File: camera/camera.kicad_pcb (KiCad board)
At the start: 4 copper layers, 45.2 x 32.5 mm, 76 parts, among them J1 Gecko, J2 USB_B_Micro, J3 Programmer, J4 OV5640, J5 Micro_SD_Card, U1 INA180, U2 TPS562200, U3 MCP2562, U4 STM32H750VBTx, U5 TLV70215_SOT23-5, U6 AP2171W, X1 ECS-2520MV-240-BN

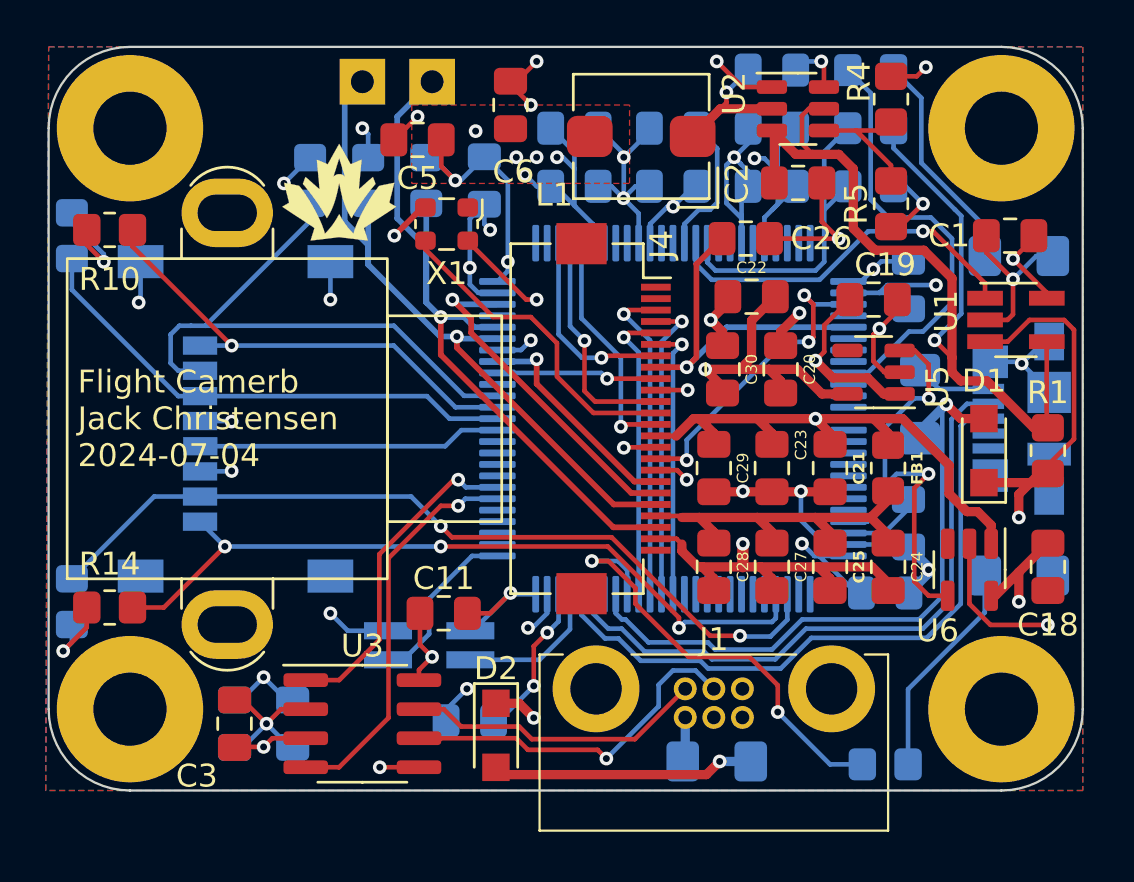
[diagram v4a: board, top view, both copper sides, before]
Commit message: Changed connector, updated board layout
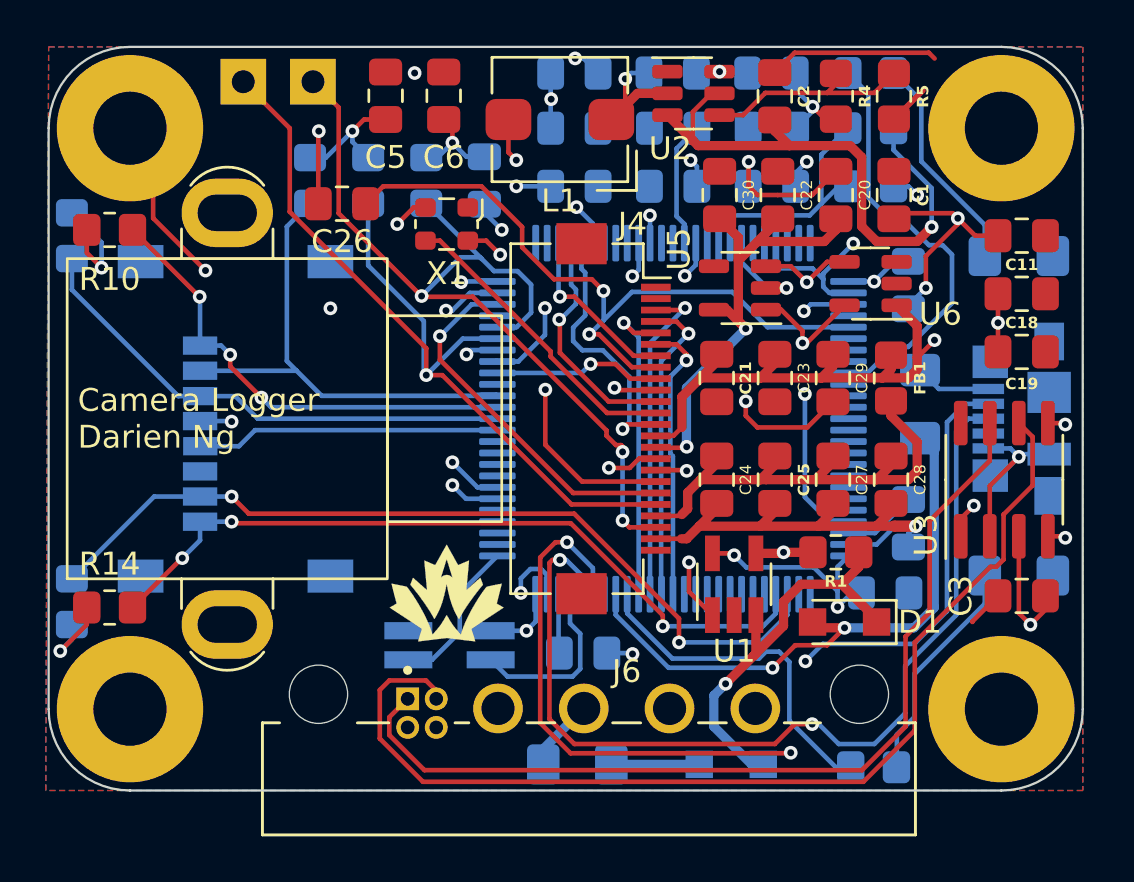
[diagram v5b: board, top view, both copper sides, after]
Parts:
- removed J1: Gecko, canhw_footprints:connector_Harwin_G125–MG10605M4P
- added J6: G125-MH104M4-04AD000P, canhw_footprints:connector_Harwin_G125-MH104M4-04AD000P, F.Cu at (179.6, 115.8)
- D2: moved to B.Cu
- moved C31 36.9 mm to (187.6, 85.0), turned to 180 degrees
- moved C3 34.9 mm to (198.5, 107.8), turned to 180 degrees
- moved C32 31.0 mm to (178.9, 85.0), turned to 0 degrees
- moved C11 30.2 mm to (198.5, 92.1), turned to 0 degrees
- moved U3 30.0 mm to (197.7, 102.7), turned to 90 degrees
- moved G*** 18.1 mm to (173.4, 107.7)
- moved C26 17.7 mm to (168.8, 90.7), turned to 180 degrees
- moved U1 16.9 mm to (185.9, 107.3), turned to 90 degrees
- moved U6 13.2 mm to (191.9, 94.2), turned to 180 degrees
- moved C18 12.0 mm to (198.5, 94.6), turned to 0 degrees
- moved D2 10.4 mm to (185.8, 115.2), turned to 180 degrees
- moved R1 10.3 mm to (190.4, 105.9), turned to 180 degrees
- moved D1 9.66 mm to (190.8, 109.0), turned to 180 degrees
- moved C28 8.63 mm to (192.8, 102.7)
- moved C24 8.41 mm to (185.2, 102.7)
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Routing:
- net GND: track 115.4 -> 72.1 mm, vias 34 -> 21
- net /CANL: track 16.7 -> 46.4 mm, vias 1 -> 0
- net Net-(D1-K): track 47.7 -> 18.2 mm, vias 2 -> 1
- net /CANH: track 13.1 -> 40.7 mm
- net /USB_D-: track 28.2 -> 44.7 mm, vias 0 -> 3
- net /CAN_TX: track 14.3 -> 30.2 mm, vias 1 -> 2
- net /MCU/PIXCLK: track 15.4 -> 30.7 mm, vias 1 -> 2
- net /CAN_RX: track 17.3 -> 32.6 mm, vias 1 -> 2
- net /USB_D+: track 28.7 -> 41.6 mm, vias 0 -> 2
- net /MCU/SCL: track 30.4 -> 40.9 mm
- net /CURR_SENS: track 16.3 -> 25.7 mm, vias 1 -> 2
- net +2V8: track 85.2 -> 75.9 mm
- net Net-(D2-A): track 11.5 -> 3.84 mm, vias 1 -> 0
- net /MCU/SDA: track 32.9 -> 40.2 mm, vias 1 -> 3
- net /MCU/VSYNC: track 9.82 -> 15.3 mm, vias 1 -> 2
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- removed copper zone on F.Cu, net +2V8
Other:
- board text added: "Camera Logger Darien Ng"
- board text removed: "Flight Camerb Jack Christensen 2024-07-04"

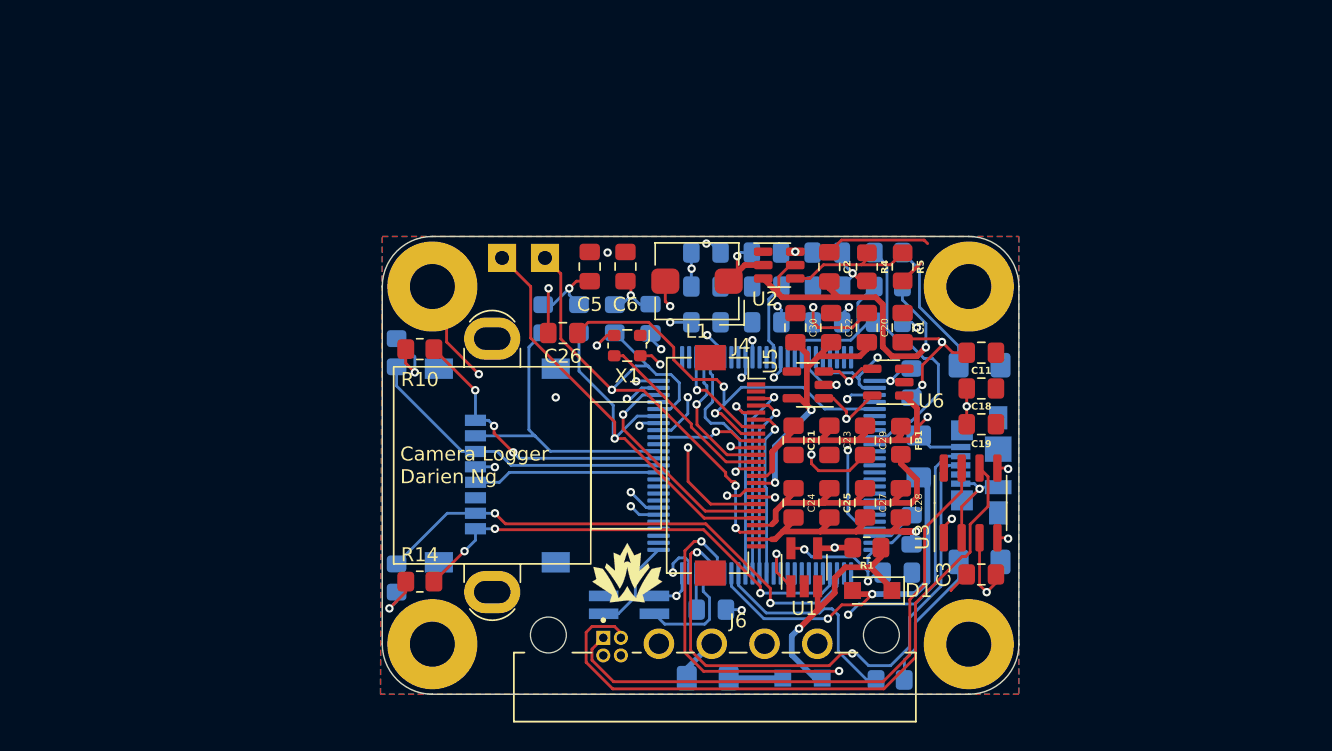
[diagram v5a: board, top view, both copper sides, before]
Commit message: Removed SCL/SDA (camera remnants), started layout
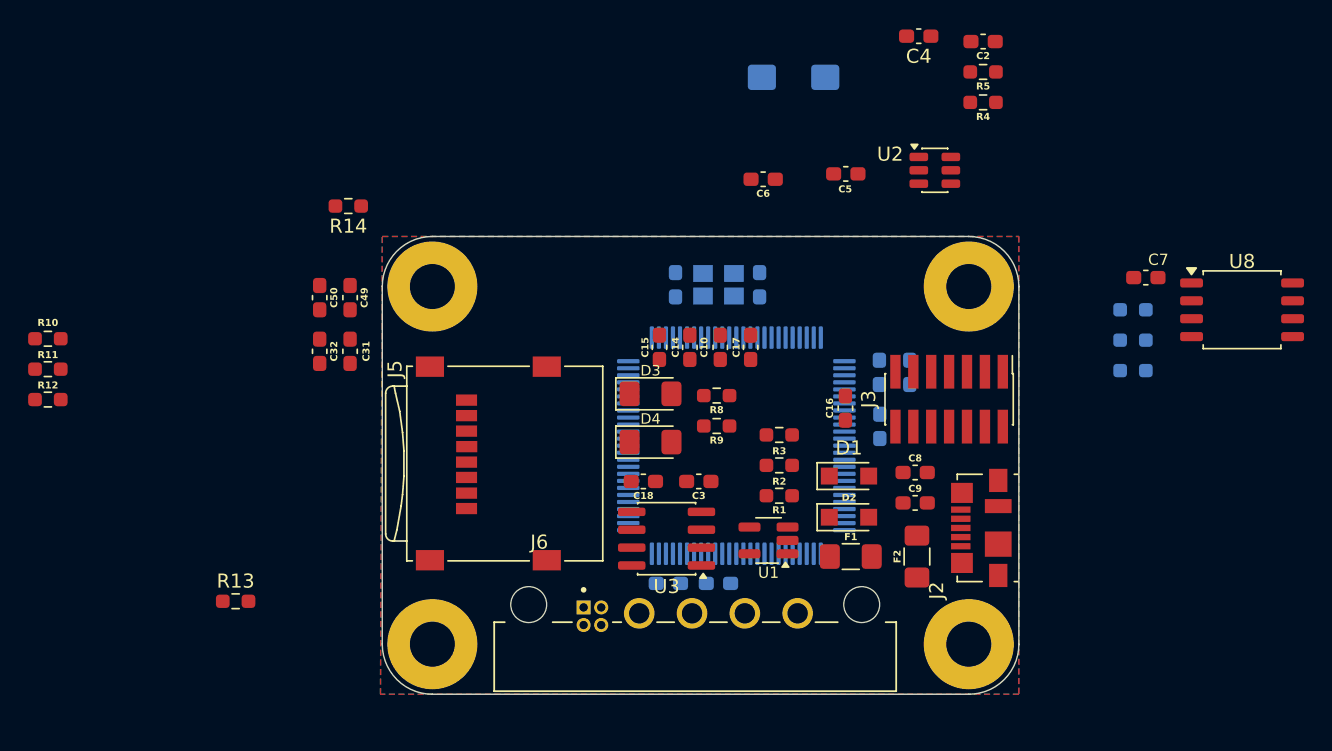
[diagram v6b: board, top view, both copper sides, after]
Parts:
- removed C21, C24, C28, C29, C30: 100n, Capacitor_SMD:C_0805_2012Metric_Pad1.18x1.45mm_HandSolder
- removed C22, C23, C25: 10u, Capacitor_SMD:C_0805_2012Metric_Pad1.18x1.45mm_HandSolder
- removed C26: 15p, Capacitor_SMD:C_0805_2012Metric_Pad1.18x1.45mm_HandSolder
- removed C27: 1u, Capacitor_SMD:C_0805_2012Metric_Pad1.18x1.45mm_HandSolder
- removed CAM1: OV5640, canhw_footprints:OV5640
- removed FB1: BLM21PG221SN1D, Resistor_SMD:R_0805_2012Metric_Pad1.20x1.40mm_HandSolder
- removed G***: LOGO, Team_Logo:Logo_SilkScreen_5mm
- removed J4: OV5640, Connector_FFC-FPC:Hirose_FH12-24S-0.5SH_1x24-1MP_P0.50mm_Horizontal
- removed NT1: NetTie_2, NetTie:NetTie-2_SMD_Pad0.5mm
- removed R6, R7: 4.7k, Resistor_SMD:R_0805_2012Metric_Pad1.20x1.40mm_HandSolder
- removed TP4: SCL, TestPoint:TestPoint_THTPad_2.0x2.0mm_Drill1.0mm
- removed TP5: SDA, TestPoint:TestPoint_THTPad_2.0x2.0mm_Drill1.0mm
- removed U5: TLV70215_SOT23-5, Package_TO_SOT_SMD:SOT-23-5
- removed U6: AP2171W, Package_TO_SOT_SMD:SOT-23-5
- removed X1: ECS-2520MV-240-BN, Oscillator:Oscillator_SMD_ECS_2520MV-xxx-xx-4Pin_2.5x2.0mm
- added C49: 1uF, Capacitor_SMD:C_0603_1608Metric_Pad1.08x0.95mm_HandSolder, F.Cu at (153.7, 88.2)
- added C50: 0.1uF, Capacitor_SMD:C_0603_1608Metric_Pad1.08x0.95mm_HandSolder, F.Cu at (151.5, 88.2)
- added R47: 10k, Resistor_SMD:R_0603_1608Metric_Pad0.98x0.95mm_HandSolder, B.Cu at (209.3, 91.2)
- added R48: 10k, Resistor_SMD:R_0603_1608Metric_Pad0.98x0.95mm_HandSolder, B.Cu at (209.3, 93.3)
- added R49: 10k, Resistor_SMD:R_0603_1608Metric_Pad0.98x0.95mm_HandSolder, B.Cu at (209.3, 89.0)
- added U8: MX25L25645GM2I-08G, Package_SO:SOIC-8_5.3x5.3mm_P1.27mm, F.Cu at (217.0, 89.0)
- added Y1: ABM8G-32.000MHZ-B4Y-T, Crystal:Crystal_SMD_Abracon_ABM8AIG-4Pin_3.2x2.5mm, B.Cu at (179.8, 87.2)
- C1, C11: footprint Capacitor_SMD:C_0805_2012Metric_Pad1.18x1.45mm_HandSolder -> Capacitor_SMD:C_0603_1608Metric_Pad1.08x0.95mm_HandSolder; moved to B.Cu
- C10, C14, C15, C16, C17, C31, C32, C4, C7, C8, C9: footprint Capacitor_SMD:C_0805_2012Metric_Pad1.18x1.45mm_HandSolder -> Capacitor_SMD:C_0603_1608Metric_Pad1.08x0.95mm_HandSolder; moved to F.Cu
- C12, C13, C2, C33, C5, C6: footprint Capacitor_SMD:C_0805_2012Metric_Pad1.18x1.45mm_HandSolder -> Capacitor_SMD:C_0603_1608Metric_Pad1.08x0.95mm_HandSolder
- C18: value 100n -> 0.1u; footprint Capacitor_SMD:C_0805_2012Metric_Pad1.18x1.45mm_HandSolder -> Capacitor_SMD:C_0603_1608Metric_Pad1.08x0.95mm_HandSolder
- C19, C20: value 1u -> 27p; footprint Capacitor_SMD:C_0805_2012Metric_Pad1.18x1.45mm_HandSolder -> Capacitor_SMD:C_0603_1608Metric_Pad1.08x0.95mm_HandSolder; moved to B.Cu
- C3: value 10u -> 0.1u; footprint Capacitor_SMD:C_0805_2012Metric_Pad1.18x1.45mm_HandSolder -> Capacitor_SMD:C_0603_1608Metric_Pad1.08x0.95mm_HandSolder
- D2, D3, D4, F1, F2, J2, J5: moved to F.Cu
- J3: footprint Connector_PinSocket_1.27mm:PinSocket_2x02_P1.27mm_Vertical_SMD -> Connector_PinHeader_1.27mm:PinHeader_2x07_P1.27mm_Vertical_SMD; moved to F.Cu
- L1: moved to B.Cu
- R1, R10, R14, R4, R5: footprint Resistor_SMD:R_0805_2012Metric_Pad1.20x1.40mm_HandSolder -> Resistor_SMD:R_0603_1608Metric_Pad0.98x0.95mm_HandSolder
- R11, R12, R13, R2, R3, R8, R9: footprint Resistor_SMD:R_0805_2012Metric_Pad1.20x1.40mm_HandSolder -> Resistor_SMD:R_0603_1608Metric_Pad0.98x0.95mm_HandSolder; moved to F.Cu
- moved H2 45.8 mm to (197.6, 87.4)
- moved H3 45.8 mm to (159.5, 112.8)
- moved R11 35.4 mm to (132.2, 93.2), turned to 0 degrees
- moved C31 34.6 mm to (153.7, 92.0), turned to -90 degrees
- moved C32 28.3 mm to (151.5, 92.0), turned to -90 degrees
- moved R14 27.1 mm to (153.5, 81.7), turned to 180 degrees
- moved J3 27.0 mm to (196.2, 95.4), turned to -90 degrees
- moved C7 26.9 mm to (210.2, 86.7), turned to 0 degrees
- moved R10 26.4 mm to (132.2, 91.1)
- moved R12 25.0 mm to (132.2, 95.4), turned to 0 degrees
- moved C18 24.9 mm to (174.5, 101.2)
- moved D4 24.9 mm to (175.0, 98.4), turned to 0 degrees
- moved D3 23.5 mm to (175.0, 95.0), turned to 0 degrees
- moved C1 22.4 mm to (179.8, 108.5), turned to 180 degrees
- moved R9 21.8 mm to (179.7, 97.3), turned to 180 degrees
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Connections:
- C19 pad 1: +2V8 -> /XTAL_1
- C20 pad 1: /OV5640/DVDD -> /XTAL_2
- J3 pad 1: GND -> unconnected-(J3-Pin_1-Pad1)
- J3 pad 2: +2V8 -> unconnected-(J3-Pin_2-Pad2)
- J3 pad 3: /MCU/SWCLK -> +2V8
- U4 pad 12: unconnected-(U4-PH0-Pad12) -> /XTAL_2
- U4 pad 13: unconnected-(U4-PH1-Pad13) -> /XTAL_1
- U4 pad 28: /MCU/HSYNC -> unconnected-(U4-PA4-Pad28)
- U4 pad 3: /MCU/DCMI_D4 -> unconnected-(U4-PE4-Pad3)
- U4 pad 30: /MCU/PIXCLK -> unconnected-(U4-PA6-Pad30)
- U4 pad 36: unconnected-(U4-PB2-Pad36) -> /Flash/FLASH_CLK
- U4 pad 37: unconnected-(U4-PE7-Pad37) -> /Flash/FLASH_IO0
- U4 pad 38: unconnected-(U4-PE8-Pad38) -> /Flash/FLASH_IO1
- U4 pad 39: unconnected-(U4-PE9-Pad39) -> /Flash/FLASH_IO2
- U4 pad 4: /MCU/DCMI_D6 -> unconnected-(U4-PE5-Pad4)
- U4 pad 40: unconnected-(U4-PE10-Pad40) -> /Flash/FLASH_IO3
- U4 pad 47: /MCU/CAM_EN -> unconnected-(U4-PB11-Pad47)
- U4 pad 5: /MCU/DCMI_D7 -> unconnected-(U4-PE6-Pad5)
- U4 pad 63: /MCU/DCMI_D0 -> unconnected-(U4-PC6-Pad63)
- U4 pad 64: /MCU/DCMI_D1 -> unconnected-(U4-PC7-Pad64)
- U4 pad 65: /MCU/DCMI_D2 -> unconnected-(U4-PC8-Pad65)
- U4 pad 66: /MCU/DCMI_D3 -> unconnected-(U4-PC9-Pad66)
- U4 pad 79: unconnected-(U4-PC11-Pad79) -> /Flash/FLASH_NCS
- U4 pad 89: /MCU/SD_D2 -> unconnected-(U4-PB3-Pad89)
- U4 pad 91: unconnected-(U4-PB5-Pad91) -> /MCU/SD_D2
- U4 pad 92: /MCU/DCMI_D5 -> unconnected-(U4-PB6-Pad92)
- U4 pad 93: /MCU/VSYNC -> unconnected-(U4-PB7-Pad93)
- U4 pad 95: /MCU/SCL -> unconnected-(U4-PB8-Pad95)
- U4 pad 96: /MCU/SDA -> unconnected-(U4-PB9-Pad96)
- U4 pad 98: /MCU/CAM_~{RESET} -> unconnected-(U4-PE1-Pad98)
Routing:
- net +2V8: track 75.9 -> 0.00 mm, vias 23 -> 0
- net GND: track 72.1 -> 0.00 mm, vias 21 -> 0
- net /CANL: track 46.4 -> 0.00 mm
- net VDC: track 45.2 -> 0.00 mm, vias 2 -> 0
- net /OV5640/DOVDD: track 44.9 -> 0.00 mm, vias 2 -> 0
- net /USB_D-: track 44.7 -> 0.00 mm, vias 3 -> 0
- net /USB_D+: track 41.6 -> 0.00 mm, vias 2 -> 0
- net /MCU/SCL: track 40.9 -> 0.00 mm, vias 1 -> 0
- net /CANH: track 40.7 -> 0.00 mm
- net /MCU/SDA: track 40.2 -> 0.00 mm, vias 3 -> 0
- net /MCU/SD_D0: track 37.5 -> 0.00 mm, vias 2 -> 0
- net /MCU/SD_D1: track 33.5 -> 0.00 mm, vias 3 -> 0
- net /CAN_RX: track 32.6 -> 0.00 mm, vias 2 -> 0
- net /MCU/PIXCLK: track 30.7 -> 0.00 mm, vias 2 -> 0
- net /CAN_TX: track 30.2 -> 0.00 mm, vias 2 -> 0
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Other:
- board text removed: "Camera Logger Darien Ng"

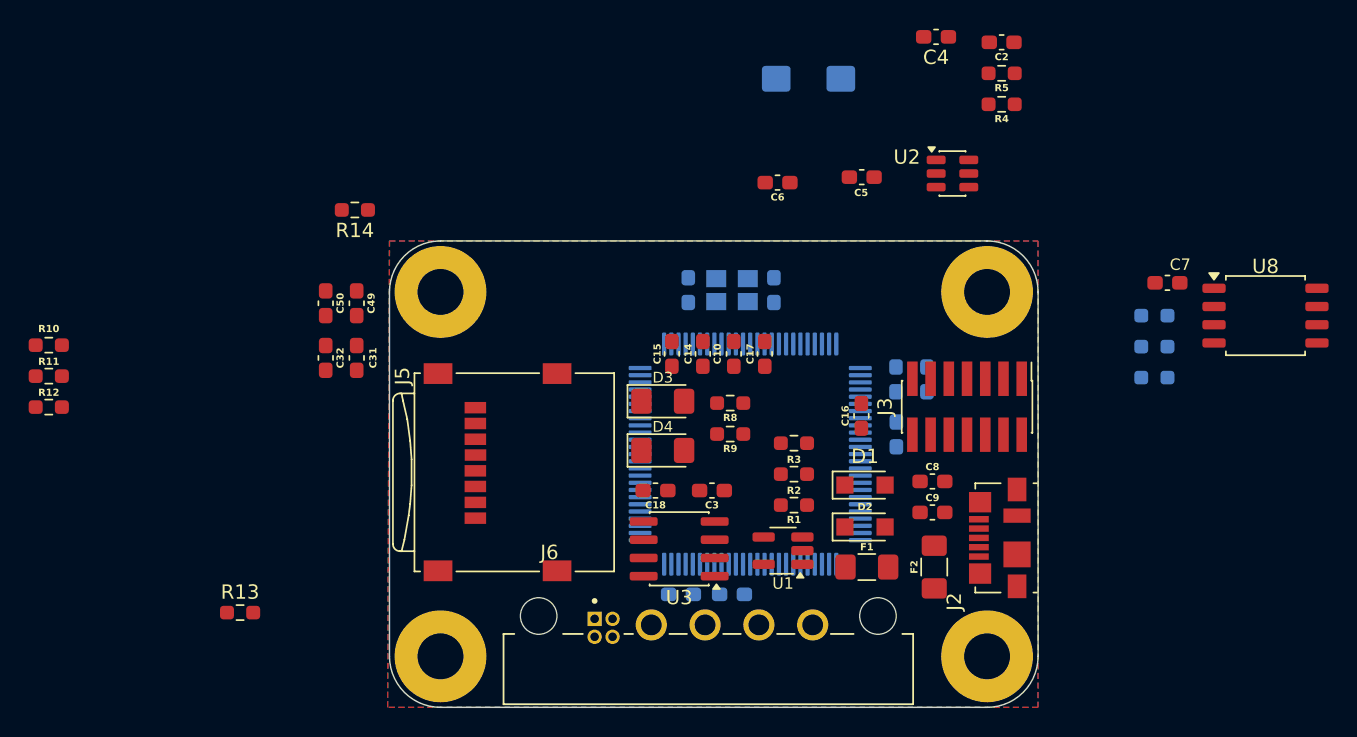
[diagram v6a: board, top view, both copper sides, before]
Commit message: Finished layout of components
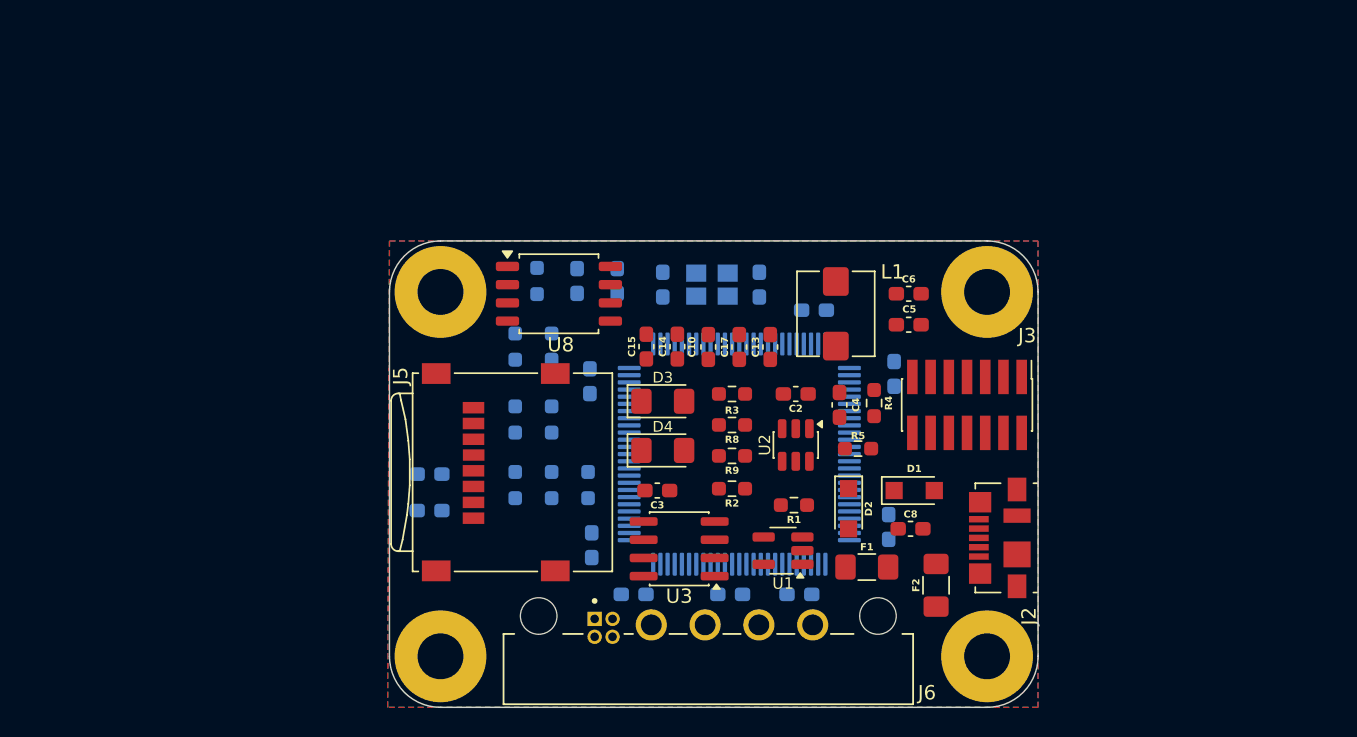
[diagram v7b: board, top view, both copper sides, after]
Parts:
- C13, L1: moved to F.Cu
- C16, C18, C31, C32, C49, C50, C7, C9, R10, R11, R12, R13, R14: moved to B.Cu
- moved U8 49.3 mm to (167.8, 87.5)
- moved R48 44.6 mm to (164.7, 91.2), turned to 90 degrees
- moved R47 43.3 mm to (166.2, 86.6), turned to -90 degrees
- moved R49 42.1 mm to (167.3, 91.2), turned to 90 degrees
- moved R10 38.8 mm to (169.8, 100.8), turned to 90 degrees
- moved R11 35.9 mm to (167.3, 100.8), turned to 90 degrees
- moved R12 33.0 mm to (164.7, 100.8), turned to 90 degrees
- moved C2 28.4 mm to (184.3, 94.5)
- moved R5 28.0 mm to (188.6, 98.3)
- moved C4 26.5 mm to (187.3, 95.2), turned to 90 degrees
- moved R13 25.6 mm to (167.3, 96.3), turned to -90 degrees
- moved C7 24.7 mm to (185.5, 88.6)
- moved R4 22.6 mm to (189.7, 95.1), turned to -90 degrees
- moved U2 21.8 mm to (184.3, 98.0), turned to -90 degrees
- moved C16 19.1 mm to (169.9, 93.6)
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
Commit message: More layout work
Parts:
- C8, U8: moved to B.Cu
- moved R47 37.8 mm to (199.6, 104.3), turned to 90 degrees
- moved R48 37.6 mm to (198.6, 107.4), turned to 180 degrees
- moved C50 31.0 mm to (199.4, 92.7), turned to 90 degrees
- moved U8 30.7 mm to (195.7, 100.2), turned to 90 degrees
- moved R49 27.3 mm to (194.6, 92.7), turned to -90 degrees
- moved C49 25.9 mm to (197.0, 92.7), turned to 90 degrees
- moved C14 8.86 mm to (168.0, 87.4)
- moved C10 8.76 mm to (170.3, 87.4)
- moved C15 8.69 mm to (166.0, 87.5)
- moved R10 7.97 mm to (162.9, 104.9)
- moved C17 5.31 mm to (175.0, 90.9), turned to 180 degrees
- moved C16 4.70 mm to (165.5, 92.1)
- moved C18 4.57 mm to (165.5, 104.9)
- moved C9 3.69 mm to (176.0, 108.3)
- moved R4 3.58 mm to (188.7, 98.6), turned to 180 degrees
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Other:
- board text added: "Note to self: do the buck transformer pours"
